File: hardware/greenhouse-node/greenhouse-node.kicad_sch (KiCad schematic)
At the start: 28 parts, among them J1 Conn_01x04_Male, J2 Conn_01x12_Male, J3 Conn_01x02_Male, J4 Conn_01x02_Male, J5 RX_PinHeader_1x04_P2.54mm, J6 TX_PinHeader_1x04_P2.54mm, Q1 BC549C, U1 ATtiny84A-P, U2 L7805, U3 74HC595

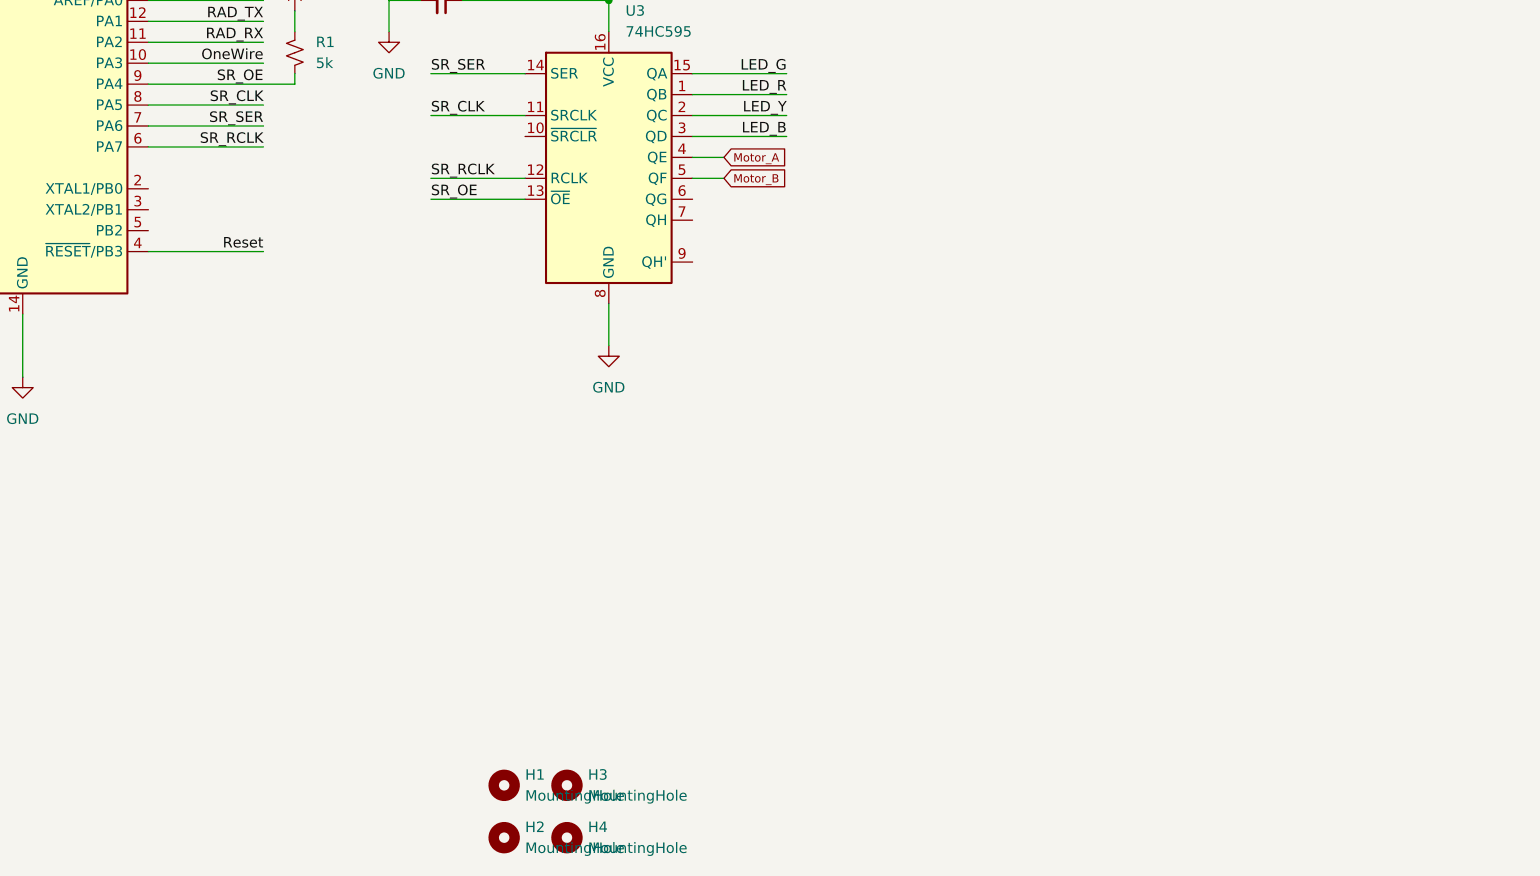
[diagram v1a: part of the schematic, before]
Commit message: Make H-bridge PWM enabled
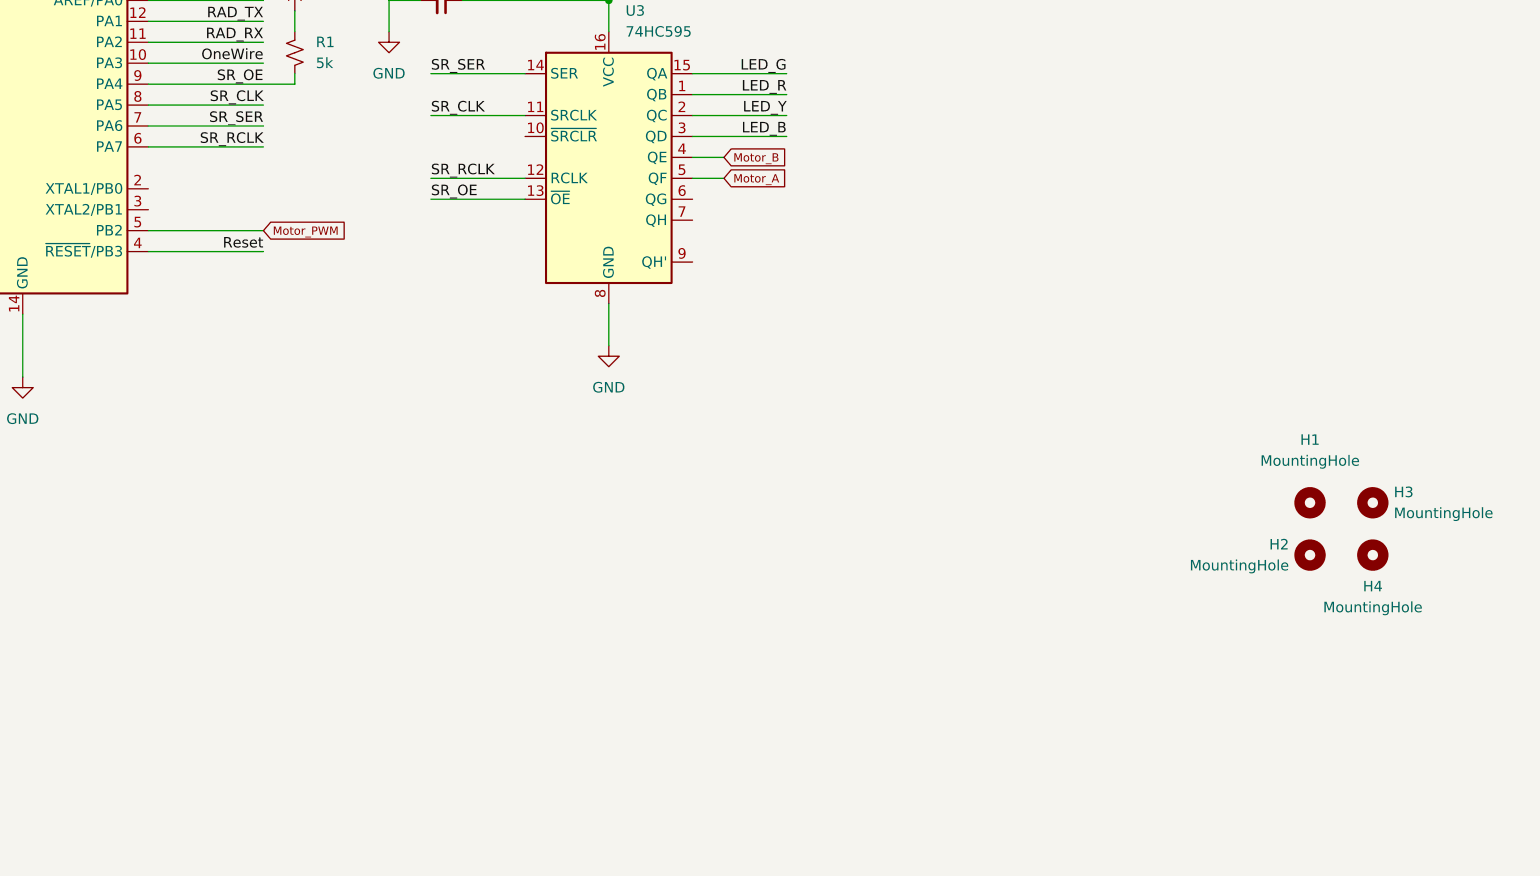
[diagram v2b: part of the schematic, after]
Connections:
- net Motor_A: now also U3.5 (QF); no longer U3.4 (QE)
- net Motor_B: now also U3.4 (QE); no longer U3.5 (QF)
- net Motor_PWM: now reaches U1.5 (PB2)
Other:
- moved on the sheet: H1, H2, H3, H4

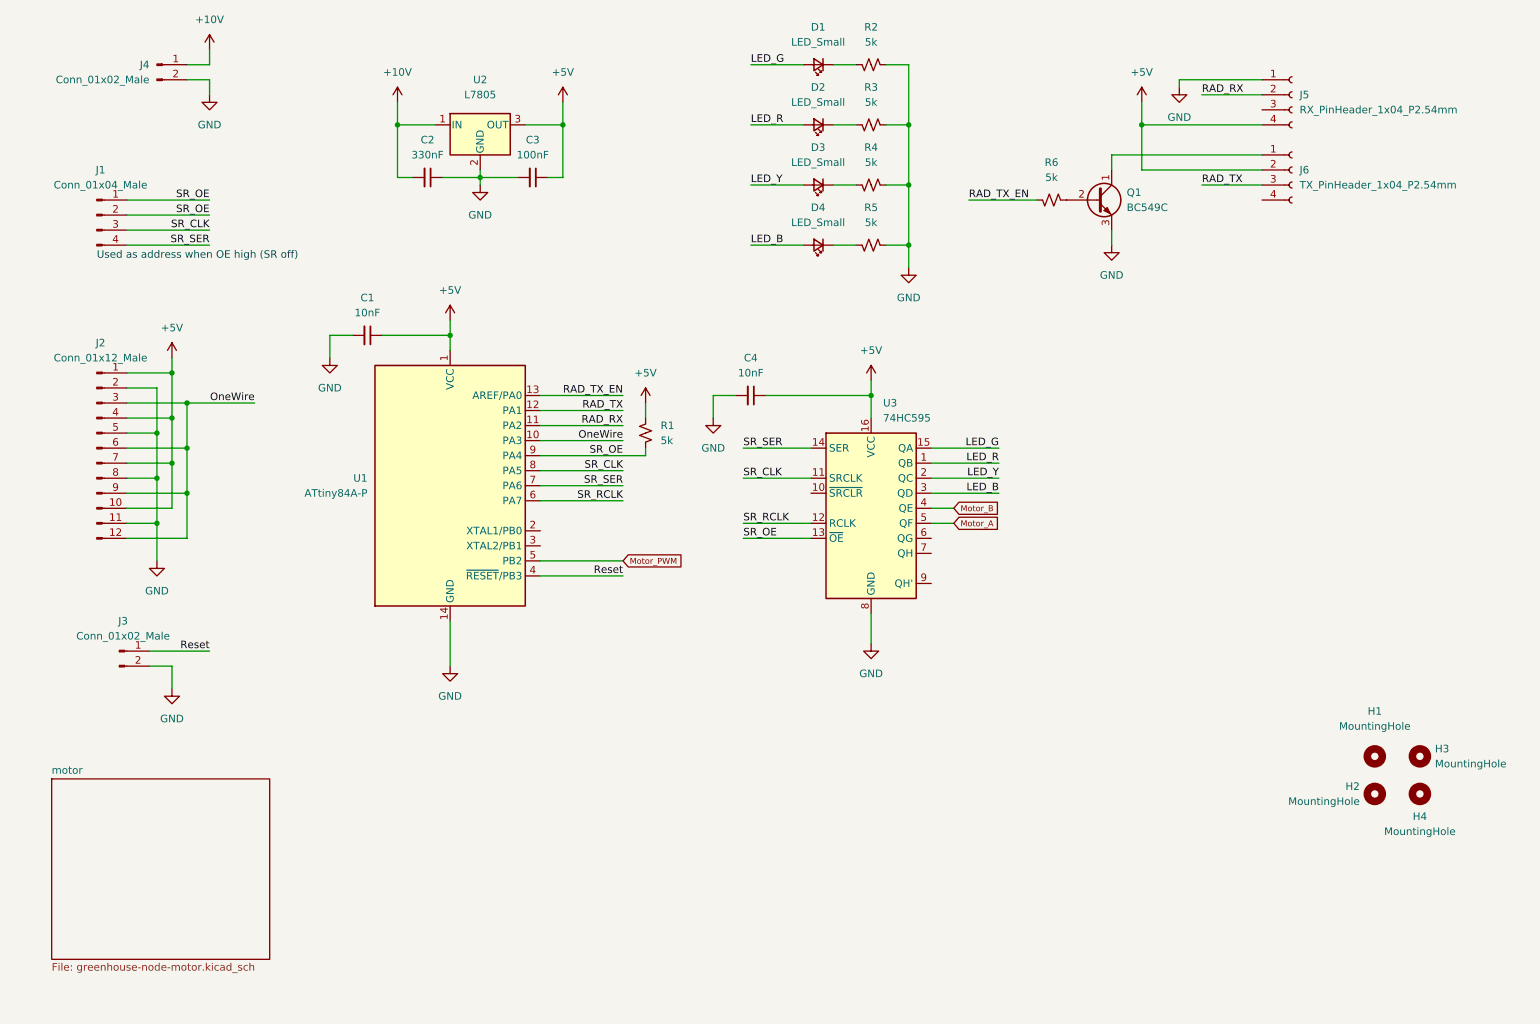
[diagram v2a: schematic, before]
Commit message: Add pull downs to SR SER+CLK
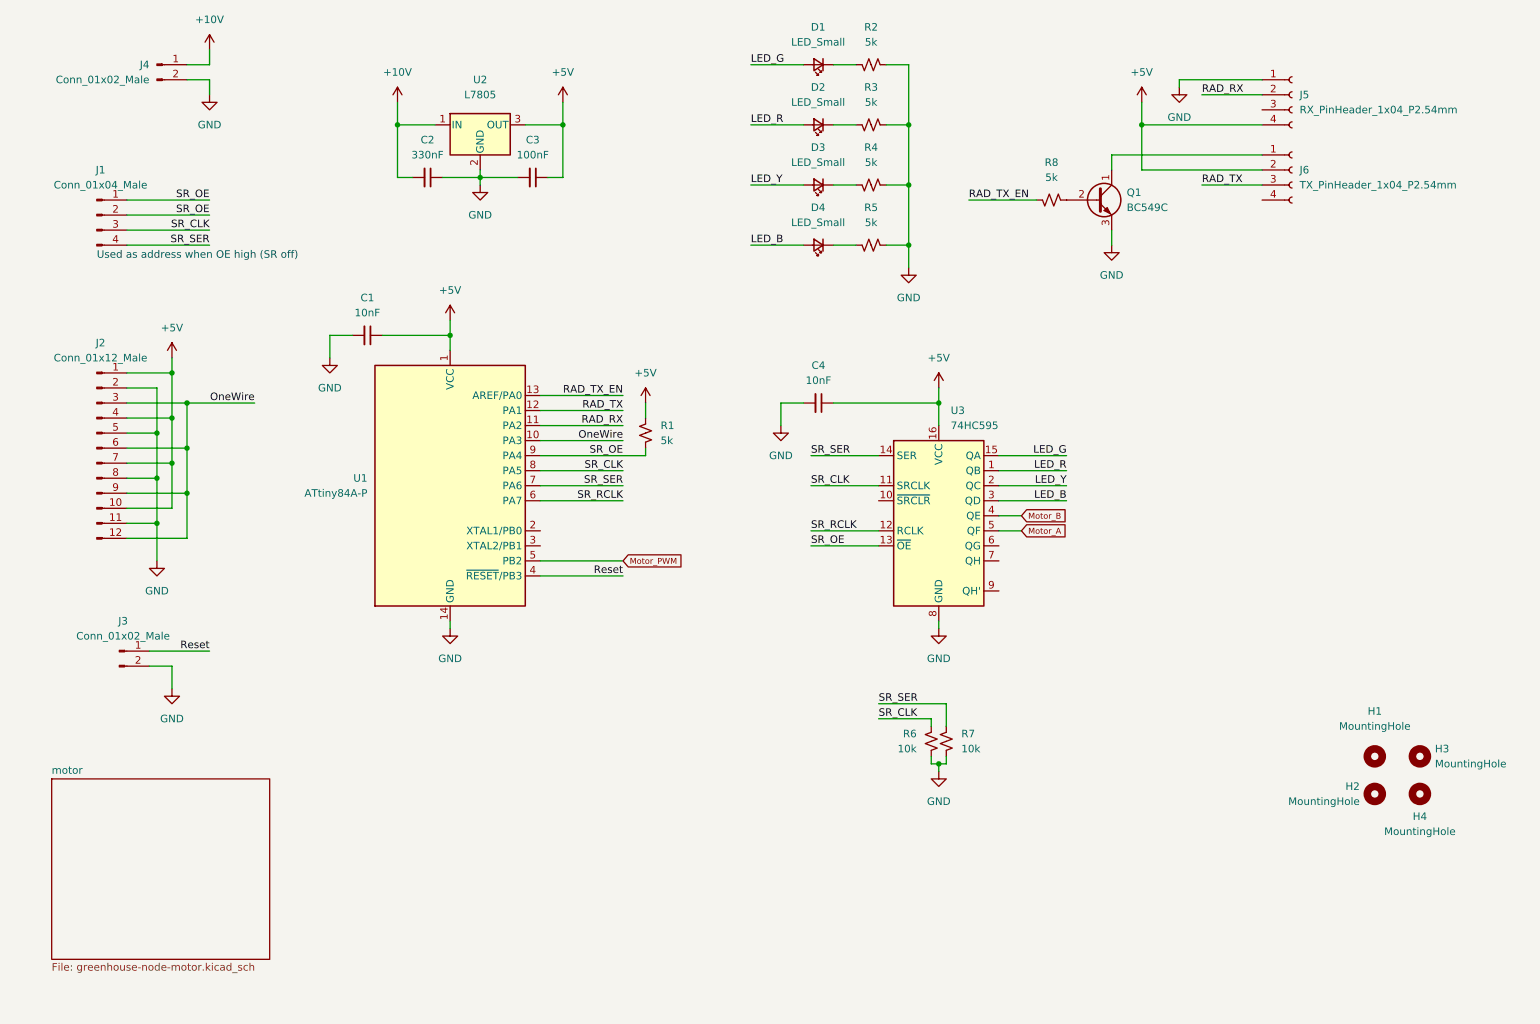
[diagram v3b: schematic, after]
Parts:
- added R6, R7: 10k, Resistor_THT:R_Axial_DIN0204_L3.6mm_D1.6mm_P7.62mm_Horizontal, symbol Device:R_Small_US
- renumbered R6 to R8
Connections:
- net GND: now also R6.1, R7.1
- net SR_CLK: now also R6.2
- net SR_SER: now also R7.2
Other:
- moved on the sheet: C4, U3
